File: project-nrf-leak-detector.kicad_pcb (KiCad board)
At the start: 2 copper layers, 56.4 x 41.4 mm, 0 parts

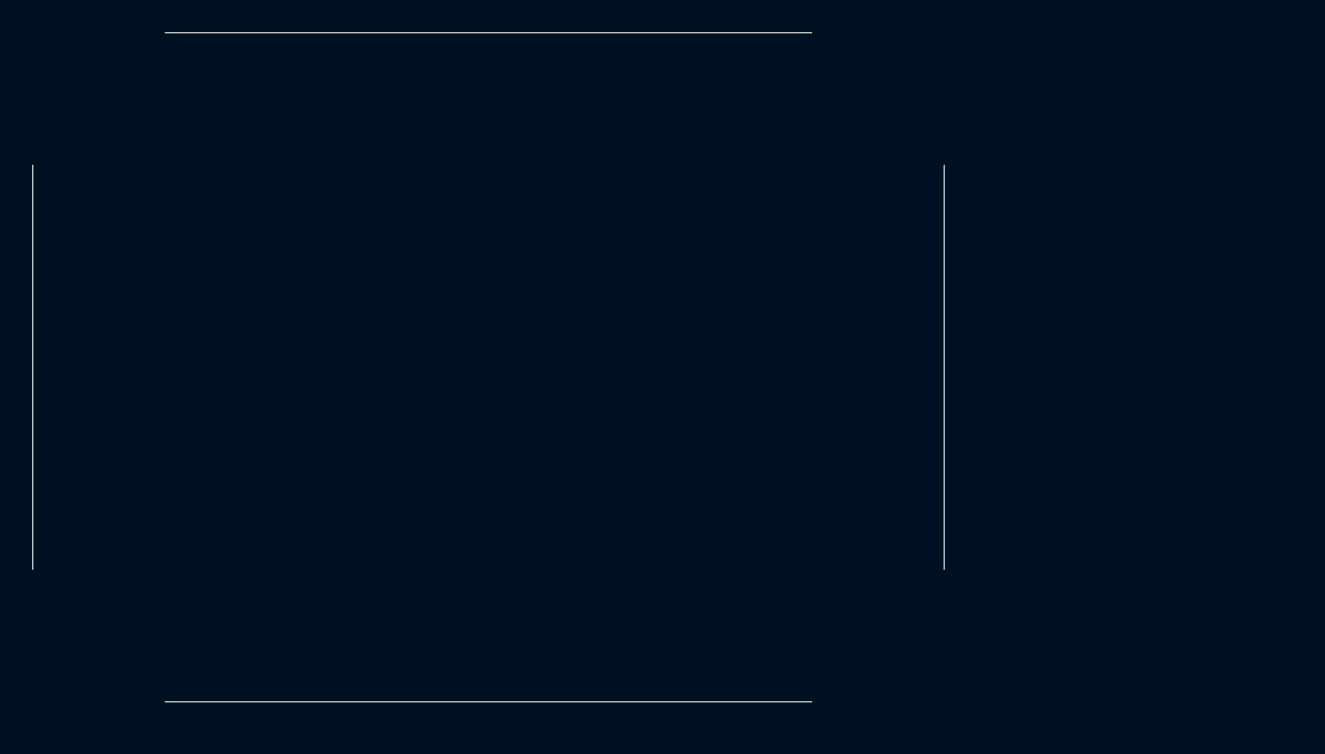
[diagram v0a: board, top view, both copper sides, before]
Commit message: Imported from project-MS88SF3-breakout schematic
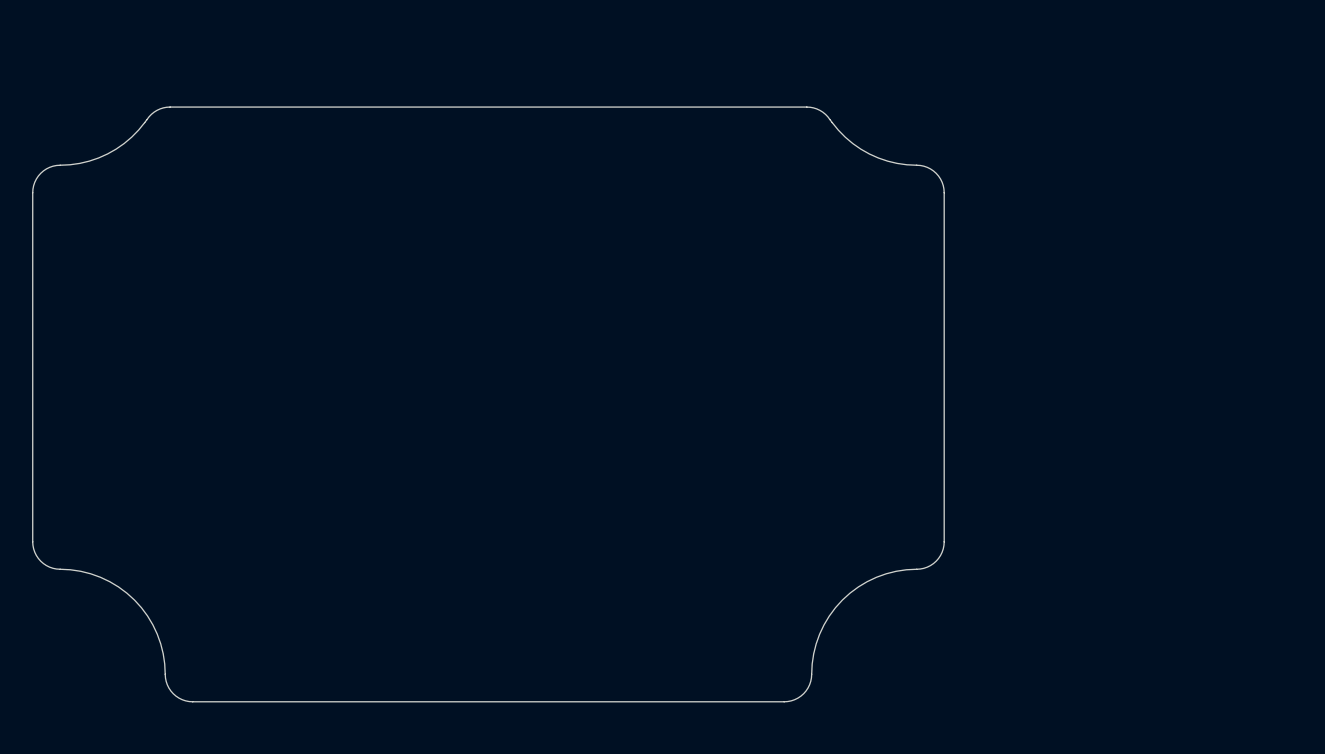
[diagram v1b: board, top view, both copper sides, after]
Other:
- board size 56.4 x 41.4 mm -> 56.4 x 36.8 mm
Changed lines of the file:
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@@
   (general
     (thickness 1.6)
-    (drawings 4)
+    (drawings 27)
     (tracks 0)
     (zones 0)
@@
     (pad_to_mask_clearance 0)
     (aux_axis_origin 0 0)
-    (grid_origin 30 30)
+    (grid_origin 58.2 50.7)
     (visible_elements FFFFFF7F)
     (pcbplotparams
@@
     (uvia_drill 0.1)
   )
-  (gr_line (start 30 38.2) (end 30 63.2) (layer Edge.Cuts) (width 0.05))
-  (gr_line (start 78.2 71.4) (end 38.2 71.4) (layer Edge.Cuts) (width 0.05))
-  (gr_line (start 86.4 38.2) (end 86.4 63.2) (layer Edge.Cuts) (width 0.05))
-  (gr_line (start 38.2 30) (end 78.2 30) (layer Edge.Cuts) (width 0.05))
+  (gr_circle (center 77.2 50.7) (end 81.25 50.7) (layer Dwgs.User) (width 0.15))
+  (gr_circle (center 39.2 50.7) (end 43.25 50.7) (layer Dwgs.User) (width 0.15))
+  (gr_circle (center 77.2 50.7) (end 79.7 50.7) (layer Dwgs.User) (width 0.15))
+  (gr_circle (center 39.2 50.7) (end 41.7 50.7) (layer Dwgs.User) (width 0.15))
+  (gr_arc (start 39.9 31.7) (end 39.9 30) (angle -90) (layer Dwgs.User) (width 0.15))
+  (gr_arc (start 31.7 31.699808) (end 36.93 35.559808) (angle 53.57083043) (layer Edge.Cuts) (width 0.05))
+  (gr_line (start 37.07 35.375622) (end 36.93 35.559808) (layer Edge.Cuts) (width 0.05))
+  (gr_arc (start 38.5 36.305622) (end 37.07 35.375622) (angle 56.9620514) (layer Edge.Cuts) (width 0.05))
+  (gr_line (start 79.33 35.375814) (end 79.47 35.56) (layer Edge.Cuts) (width 0.05))
+  (gr_arc (start 84.7 31.7) (end 79.47 35.56) (angle -53.57083043) (layer Edge.Cuts) (width 0.05))
+  (gr_arc (start 77.9 36.305814) (end 79.33 35.375814) (angle -56.9620514) (layer Edge.Cuts) (width 0.05))
+  (gr_line (start 38.5 34.599808) (end 77.9 34.6) (layer Edge.Cuts) (width 0.05))
+  (gr_arc (start 84.7 69.7) (end 84.7 63.2) (angle -90) (layer Edge.Cuts) (width 0.05))
+  (gr_arc (start 84.7 31.7) (end 78.2 31.7) (angle -90) (layer Dwgs.User) (width 0.15))
+  (gr_arc (start 31.7 31.7) (end 31.7 38.2) (angle -90) (layer Dwgs.User) (width 0.15))
+  (gr_arc (start 31.7 69.7) (end 38.2 69.7) (angle -90) (layer Edge.Cuts) (width 0.05))
+  (gr_line (start 39.9 30) (end 76.5 30) (layer Dwgs.User) (width 0.15))
+  (gr_arc (start 76.5 31.7) (end 78.2 31.7) (angle -90) (layer Dwgs.User) (width 0.15))
+  (gr_arc (start 39.9 69.7) (end 38.2 69.7) (angle -90) (layer Edge.Cuts) (width 0.05))
+  (gr_arc (start 76.5 69.7) (end 76.5 71.4) (angle -90) (layer Edge.Cuts) (width 0.05))
+  (gr_line (start 86.4 61.5) (end 86.4 39.9) (layer Edge.Cuts) (width 0.05))
+  (gr_arc (start 84.7 39.9) (end 86.4 39.9) (angle -90) (layer Edge.Cuts) (width 0.05))
+  (gr_arc (start 84.7 61.5) (end 84.7 63.2) (angle -90) (layer Edge.Cuts) (width 0.05))
+  (gr_arc (start 31.7 61.5) (end 30 61.5) (angle -90) (layer Edge.Cuts) (width 0.05))
+  (gr_arc (start 31.7 39.9) (end 31.7 38.2) (angle -90) (layer Edge.Cuts) (width 0.05))
+  (gr_line (start 30 39.9) (end 30 61.5) (layer Edge.Cuts) (width 0.05))
+  (gr_line (start 76.5 71.4) (end 39.9 71.4) (layer Edge.Cuts) (width 0.05))
 )

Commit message: Import parts to board
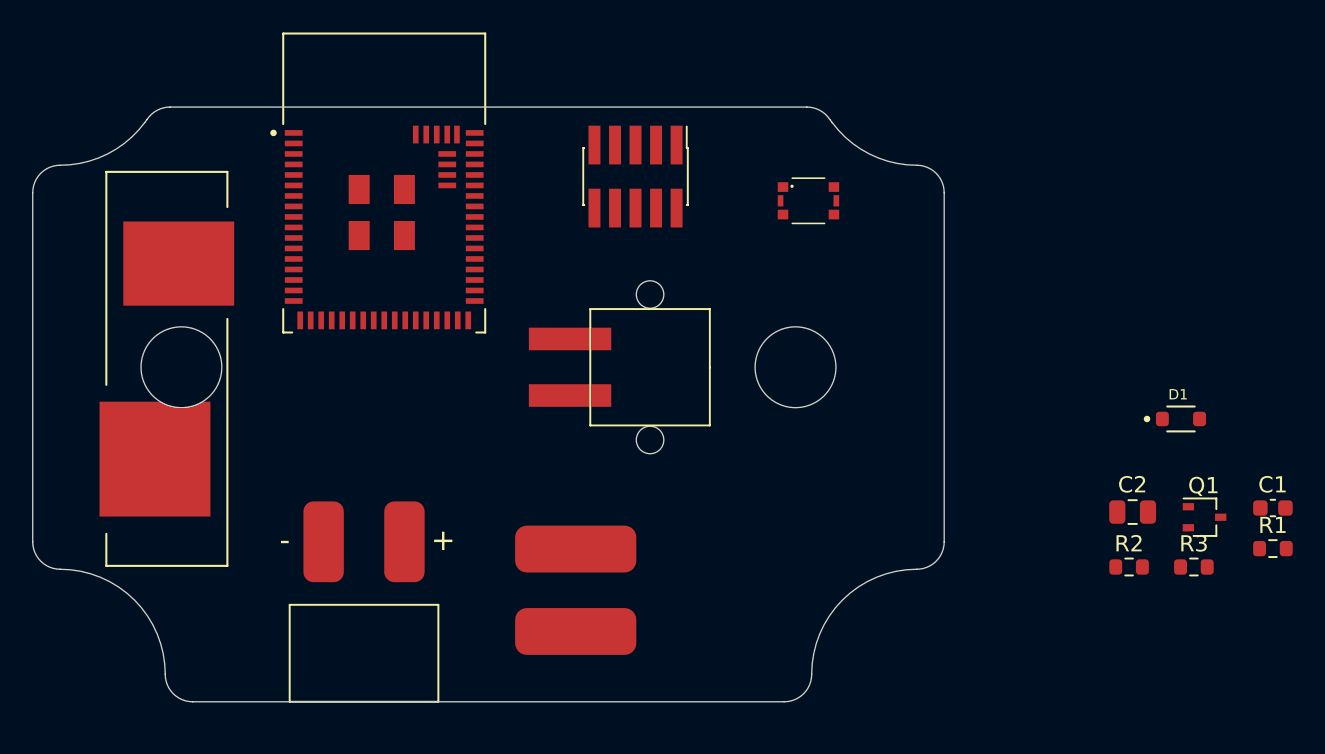
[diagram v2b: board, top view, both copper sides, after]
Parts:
- added BT1: BK-5058-SM, BK-5058-SM:BAT_BK-5058-SM, F.Cu at (38.3, 50.8)
- added C1: 100nF, Capacitor_SMD:C_0603_1608Metric, F.Cu at (106.7, 59.4)
- added C2: 4.7uF, Capacitor_SMD:C_0805_2012Metric, F.Cu at (98.1, 59.7)
- added D1: D_Schottky, CUS10S30,H3F:DIO_CUS520,H3F, F.Cu at (101.0, 53.9)
- added H1: MountingHole, MountingHole:MountingHole_5mm, F.Cu at (39.2, 50.7)
- added H2: MountingHole, MountingHole:MountingHole_5mm, F.Cu at (77.2, 50.7)
- added J1: Conn_02x05_Odd_Even, Connector_PinHeader_1.27mm:PinHeader_2x05_P1.27mm_Vertical_SMD, F.Cu at (67.3, 38.9)
- added J2: Water Probe, TZ022101B000G:TZ022101B000G, F.Cu at (68.2, 50.7)
- added L1: L, 22R686MC:INDP7870X750, F.Cu at (63.6, 64.5)
- added LS1: PKM13EPYH4000-A0, PKM13EPYH4000-A0:SPKR_PKM13EPYH4000-A0_SMD, F.Cu at (50.5, 61.5)
- added Q1: Q_NMOS_GSD, Package_TO_SOT_SMD:SOT-323_SC-70, F.Cu at (102.5, 60.0)
- added R1: 10k, Resistor_SMD:R_0603_1608Metric, F.Cu at (106.7, 61.9)
- added R2: 10k, Resistor_SMD:R_0603_1608Metric, F.Cu at (97.8, 63.1)
- added R3: 10k, Resistor_SMD:R_0603_1608Metric, F.Cu at (101.8, 63.1)
- added S1: 435151014824, 435151014824:435151014824, F.Cu at (78.0, 40.4)
- added U1: MS88SF3_NRF52840, MS88SF3_NRF52840:MODULE_MS88SF3_NRF52840, F.Cu at (51.8, 39.3)

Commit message: First placement
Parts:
- BT1: value BK-5058-SM -> BK-912-TR; footprint BK-5058-SM:BAT_BK-5058-SM -> BK-912:MPD_BK-912-TR; moved to B.Cu
- moved Q1 55.8 mm to (47.0, 54.6)
- moved R2 52.1 mm to (46.9, 52.2)
- moved D1 50.7 mm to (50.5, 57.1), turned to 270 degrees
- moved C2 42.8 mm to (56.2, 50.7)
- moved R3 41.3 mm to (61.2, 55.7)
- moved R1 39.6 mm to (76.2, 36.7)
- moved C1 37.1 mm to (76.2, 38.3), turned to 180 degrees
- moved BT1 19.9 mm to (58.2, 50.7), turned to 0 degrees
- moved S1 2.22 mm to (76.2, 41.7)
- moved LS1 1.20 mm to (50.5, 62.7)
- moved L1 0.45 mm to (63.2, 64.7), turned to 0 degrees
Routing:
- net Net-(D1-Pad2): track 0.00 -> 19.7 mm
- net VDD: track 0.00 -> 12.1 mm
- net /WATER_PROBE: track 0.00 -> 3.76 mm
- net Net-(D1-Pad1): track 0.00 -> 3.08 mm
- added copper zone on B.Cu, net GND
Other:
- board size 56.4 x 36.8 mm -> 51.3 x 36.8 mm

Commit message: First routing
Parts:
- moved R1 39.6 mm to (36.7, 40.0), turned to 90 degrees
- moved C1 37.9 mm to (38.3, 40.0), turned to 270 degrees
- moved S1 35.1 mm to (41.2, 39.7), turned to 270 degrees
- moved C2 0.20 mm to (56.0, 50.7)
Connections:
- U1 pad 16: Net-(U1-Pad16) -> /WATER_PROBE
- U1 pad 9: /WATER_PROBE -> Net-(U1-Pad9)
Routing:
- net /~RESET: track 0.00 -> 52.8 mm
- net /RX: track 0.00 -> 35.5 mm
- net /TX: track 0.00 -> 35.5 mm, vias 0 -> 2
- net /WATER_PROBE: track 3.76 -> 36.8 mm, vias 0 -> 2
- net GND: track 0.00 -> 29.9 mm, vias 0 -> 14
- net /SWDIO: track 0.00 -> 17.9 mm
- net /SWCLK: track 0.00 -> 16.0 mm
- net /BUZZER: track 0.00 -> 12.0 mm
- net VDD: track 12.1 -> 12.3 mm, vias 0 -> 10
- added copper zone on F.Cu, net GND
- added copper zone on F.Cu, net VDD
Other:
- outline, holes or cut-outs redrawn
- rule trace_min: 0.2 -> 0.127
